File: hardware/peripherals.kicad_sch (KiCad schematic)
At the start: 27 parts, among them J10 Top Left Switch, J11 Top Right Switch, J12 Bottom Left Switch, J13 Bottom Right Switch, J9 Speaker connector, U10 MAX98357A, U11 BMI088

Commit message: replacing components
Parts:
- renumbered R32 to R30, R33 to R31, R34 to R32, R35 to R33, R36 to R34, R37 to R35

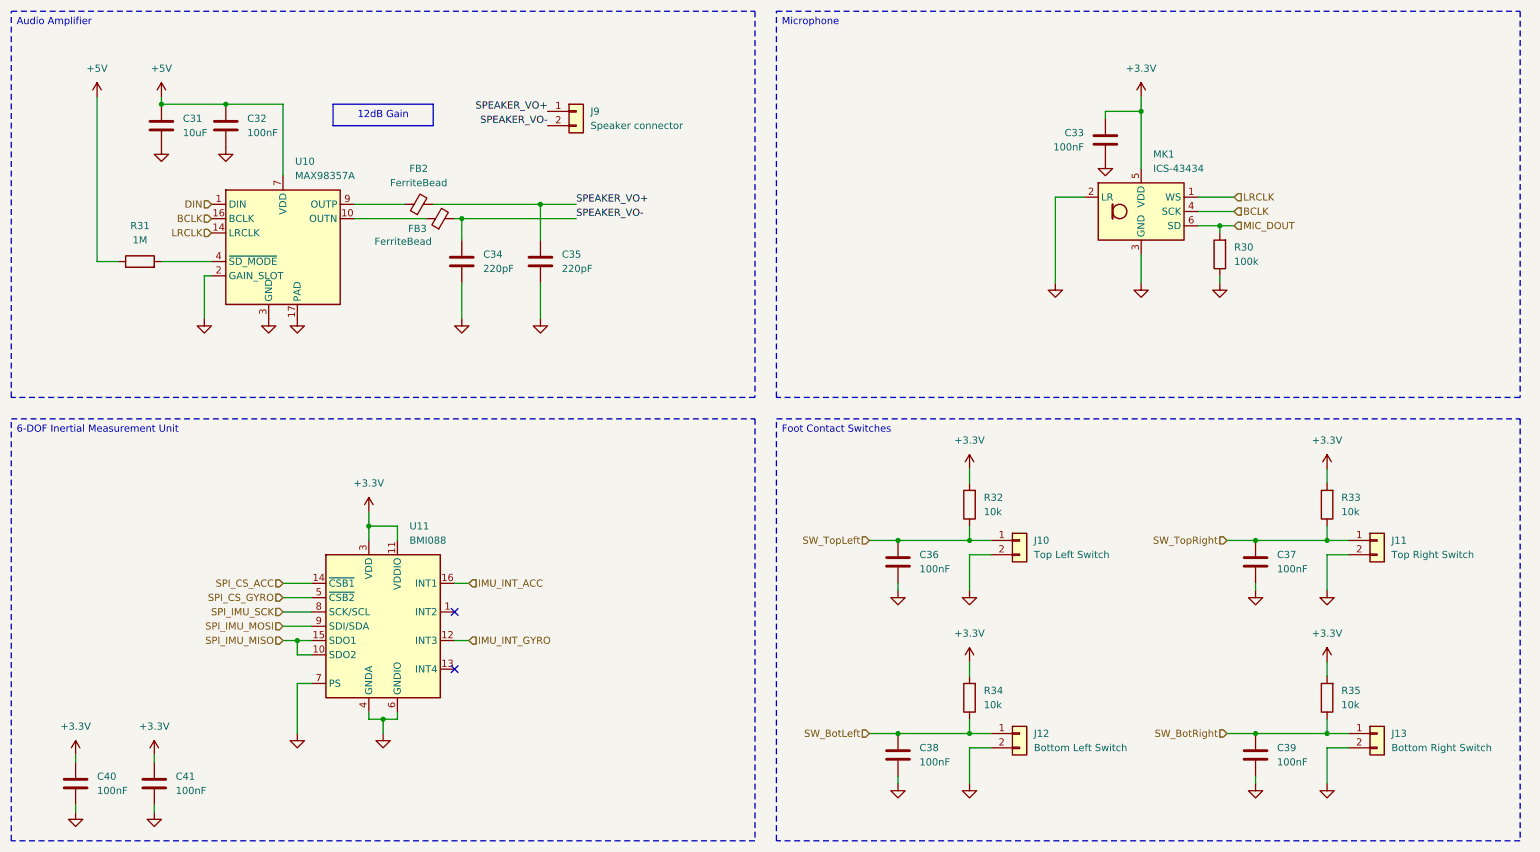
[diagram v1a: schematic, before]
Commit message: schematic update
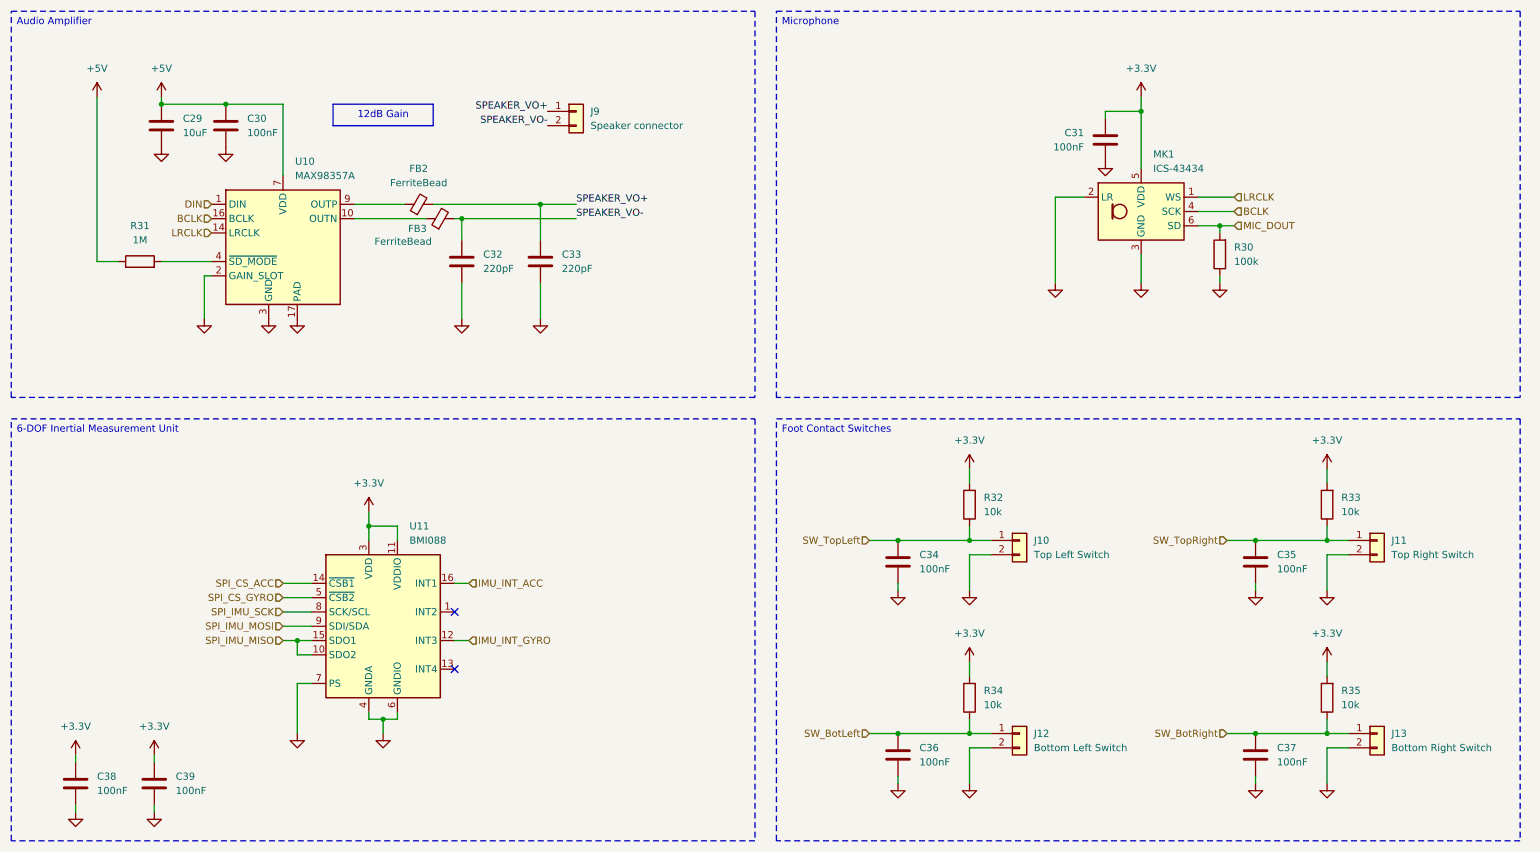
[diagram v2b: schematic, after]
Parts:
- renumbered C31 to C29, C32 to C30, C33 to C31, C34 to C32, C35 to C33, C36 to C34, C37 to C35, C38 to C36, C39 to C37, C40 to C38, C41 to C39

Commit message: update schematic
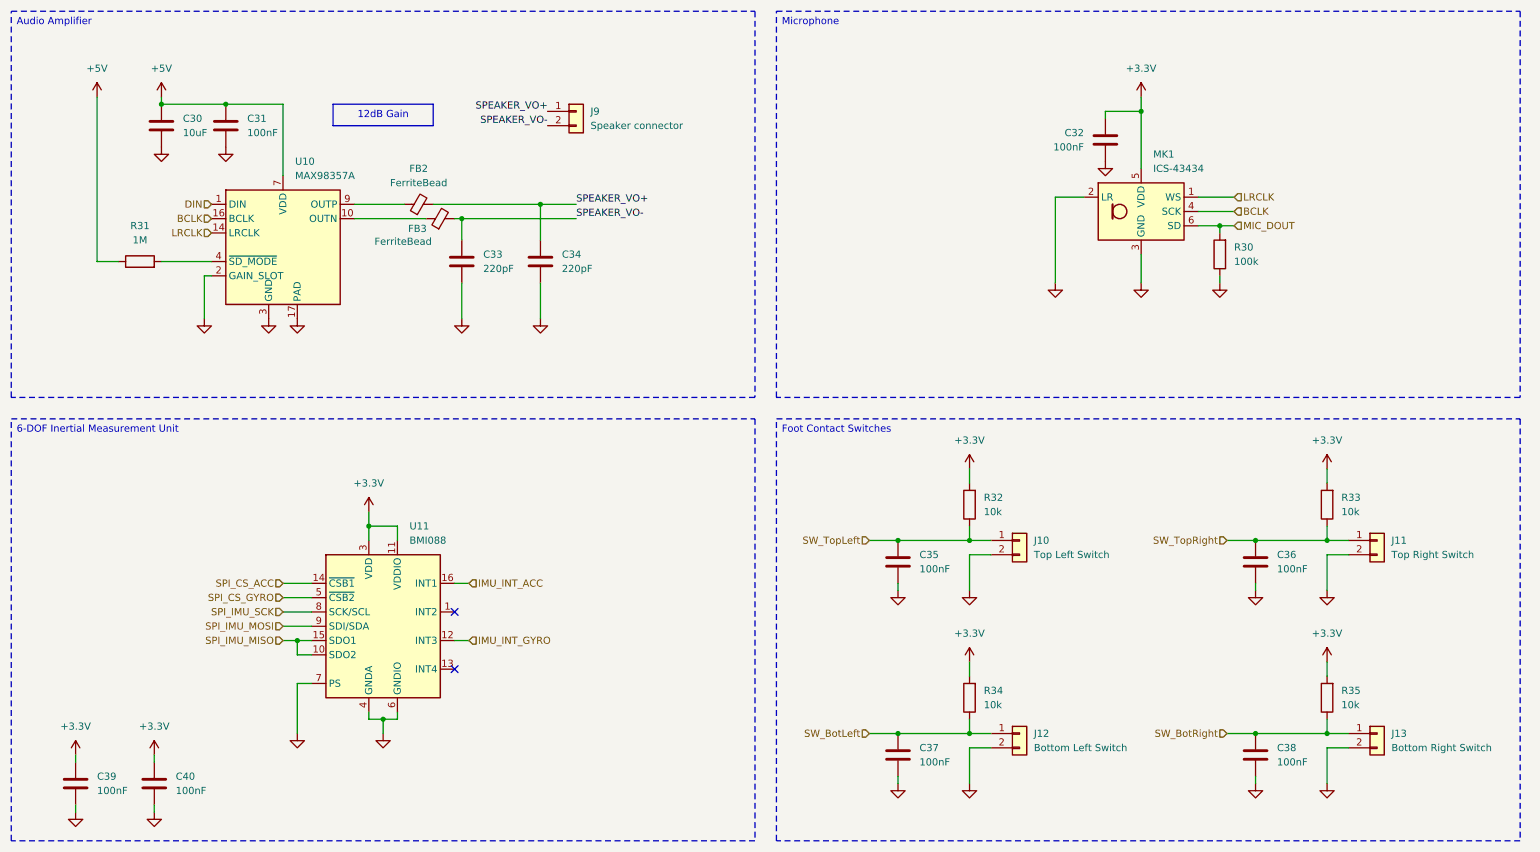
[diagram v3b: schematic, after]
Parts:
- renumbered C29 to C30, C30 to C31, C31 to C32, C32 to C33, C33 to C34, C34 to C35, C35 to C36, C36 to C37, C37 to C38, C38 to C39, C39 to C40
